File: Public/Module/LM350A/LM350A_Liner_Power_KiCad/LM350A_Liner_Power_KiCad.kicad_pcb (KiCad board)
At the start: 2 copper layers, 100 x 100 mm, 23 parts, among them J1 Screw_Terminal_01x04, J2 Screw_Terminal_01x04, J3 Screw_Terminal_01x02, SW1 SS-12D, U1 LM350_TO220

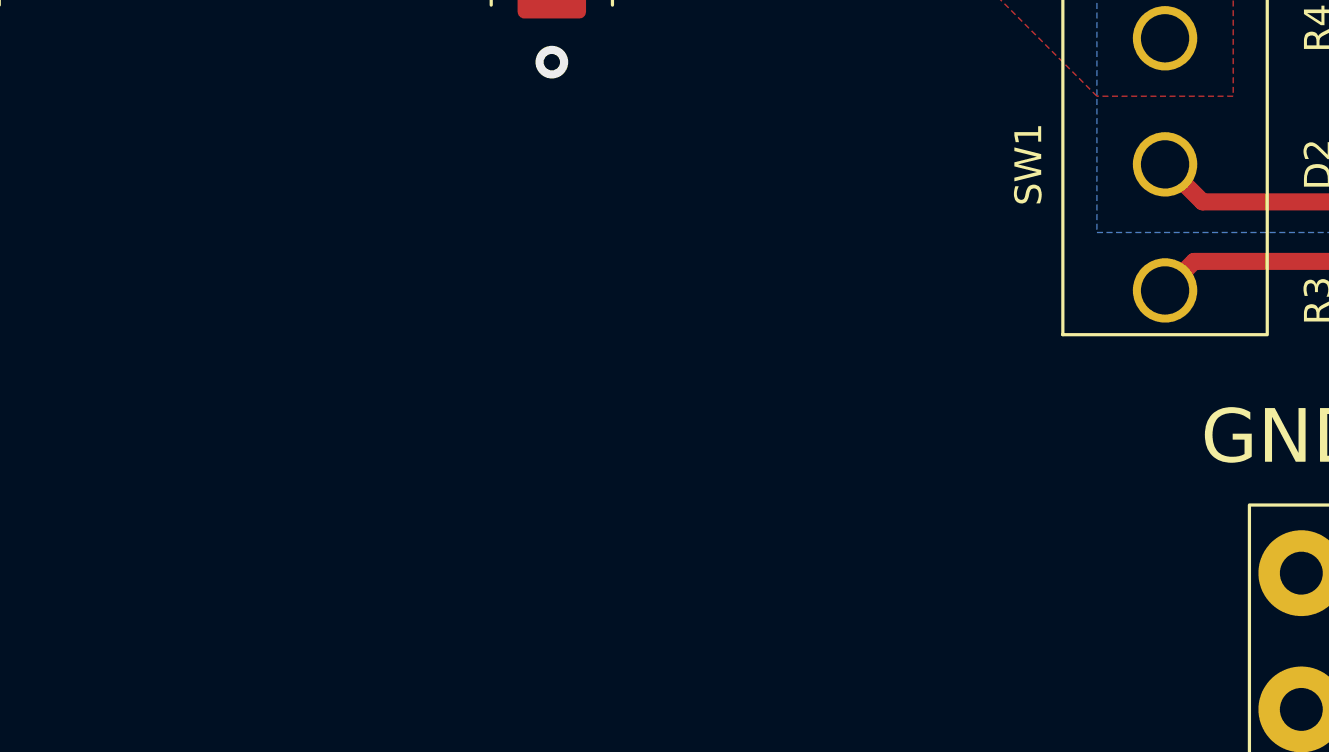
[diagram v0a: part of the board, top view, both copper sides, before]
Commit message: Update LM350A Moudle
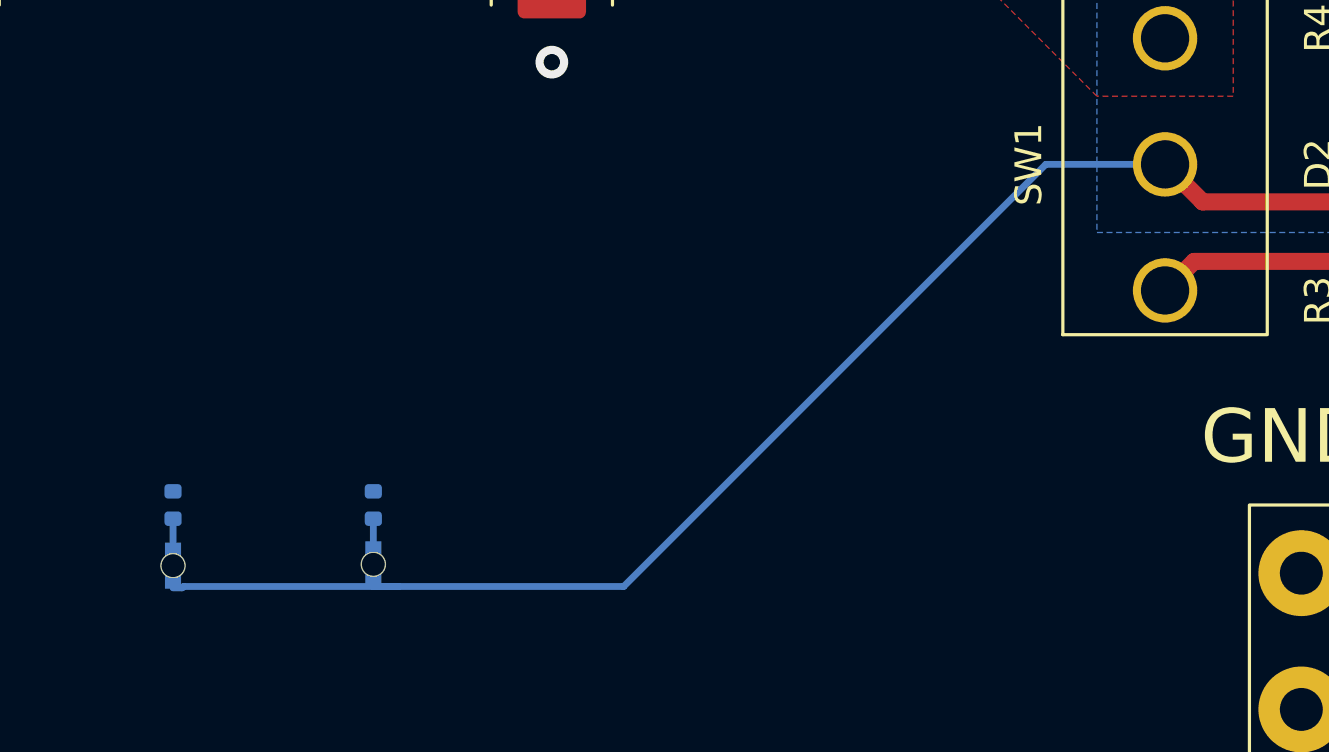
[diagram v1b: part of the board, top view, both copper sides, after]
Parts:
- added D4: LED 0402, Customer_Passive:LED_0402_Bottom, B.Cu at (148.4, 116.6)
- added D5: LED 0402, Customer_Passive:LED_0402_Bottom, B.Cu at (155.9, 116.5)
- added R5: 1k 0402, Resistor_SMD:R_0402_1005Metric, B.Cu at (148.4, 114.3)
- added R6: 1k 0402, Resistor_SMD:R_0402_1005Metric, B.Cu at (155.9, 114.3)
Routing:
- net POWER_OUT: track 8.20 -> 52.7 mm
- net Net-(D4-K): track 0.00 -> 0.92 mm
- net Net-(D5-K): track 0.00 -> 0.87 mm

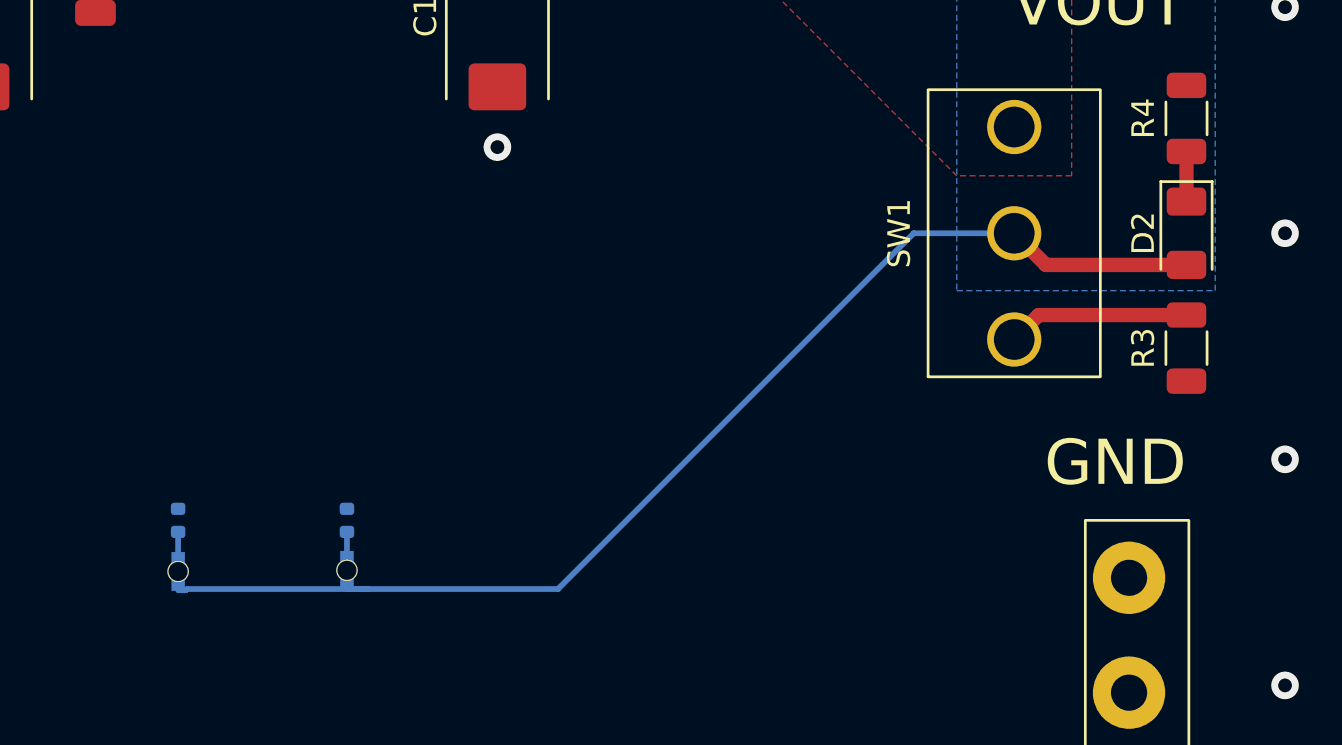
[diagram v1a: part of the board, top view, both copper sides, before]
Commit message: Update LM350 Module
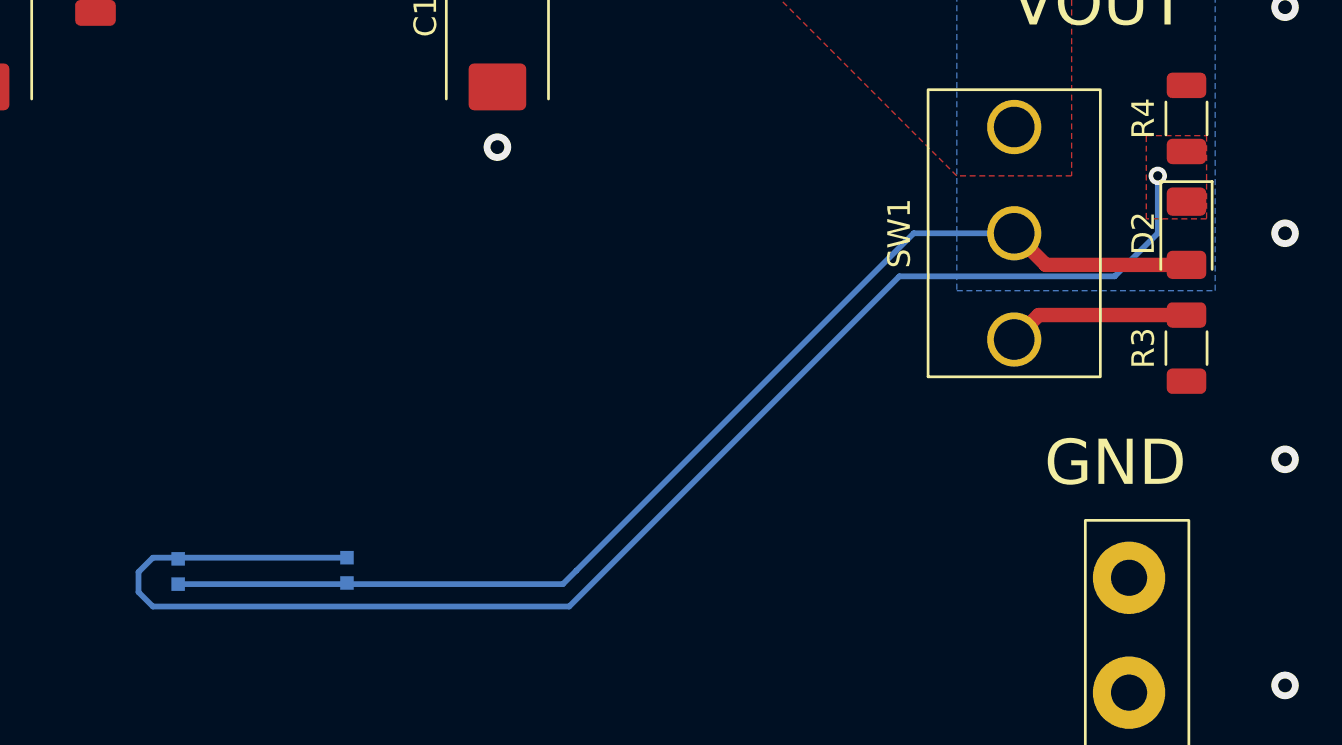
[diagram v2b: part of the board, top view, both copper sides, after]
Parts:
- removed R5, R6: 1k 0402, Resistor_SMD:R_0402_1005Metric
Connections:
- D4 pad 1: Net-(D4-K) -> Net-(D2-K)
- D5 pad 1: Net-(D5-K) -> Net-(D2-K)
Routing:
- net Net-(D2-K): track 2.22 -> 65.1 mm, vias 0 -> 1
- net POWER_OUT: track 52.7 -> 51.6 mm
- net Net-(D4-K): track 0.92 -> 0.00 mm
- net Net-(D5-K): track 0.87 -> 0.00 mm
- added copper zone on F.Cu, net Net-(D2-K)
